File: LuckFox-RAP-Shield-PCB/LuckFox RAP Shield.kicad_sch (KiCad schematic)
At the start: 4 parts, among them J1 LuckFox_Pico_Mini_Connector, J2 External_5V_Input_from_Buck_M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, U2 W5500_Ethernet_Module_DNP_on_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

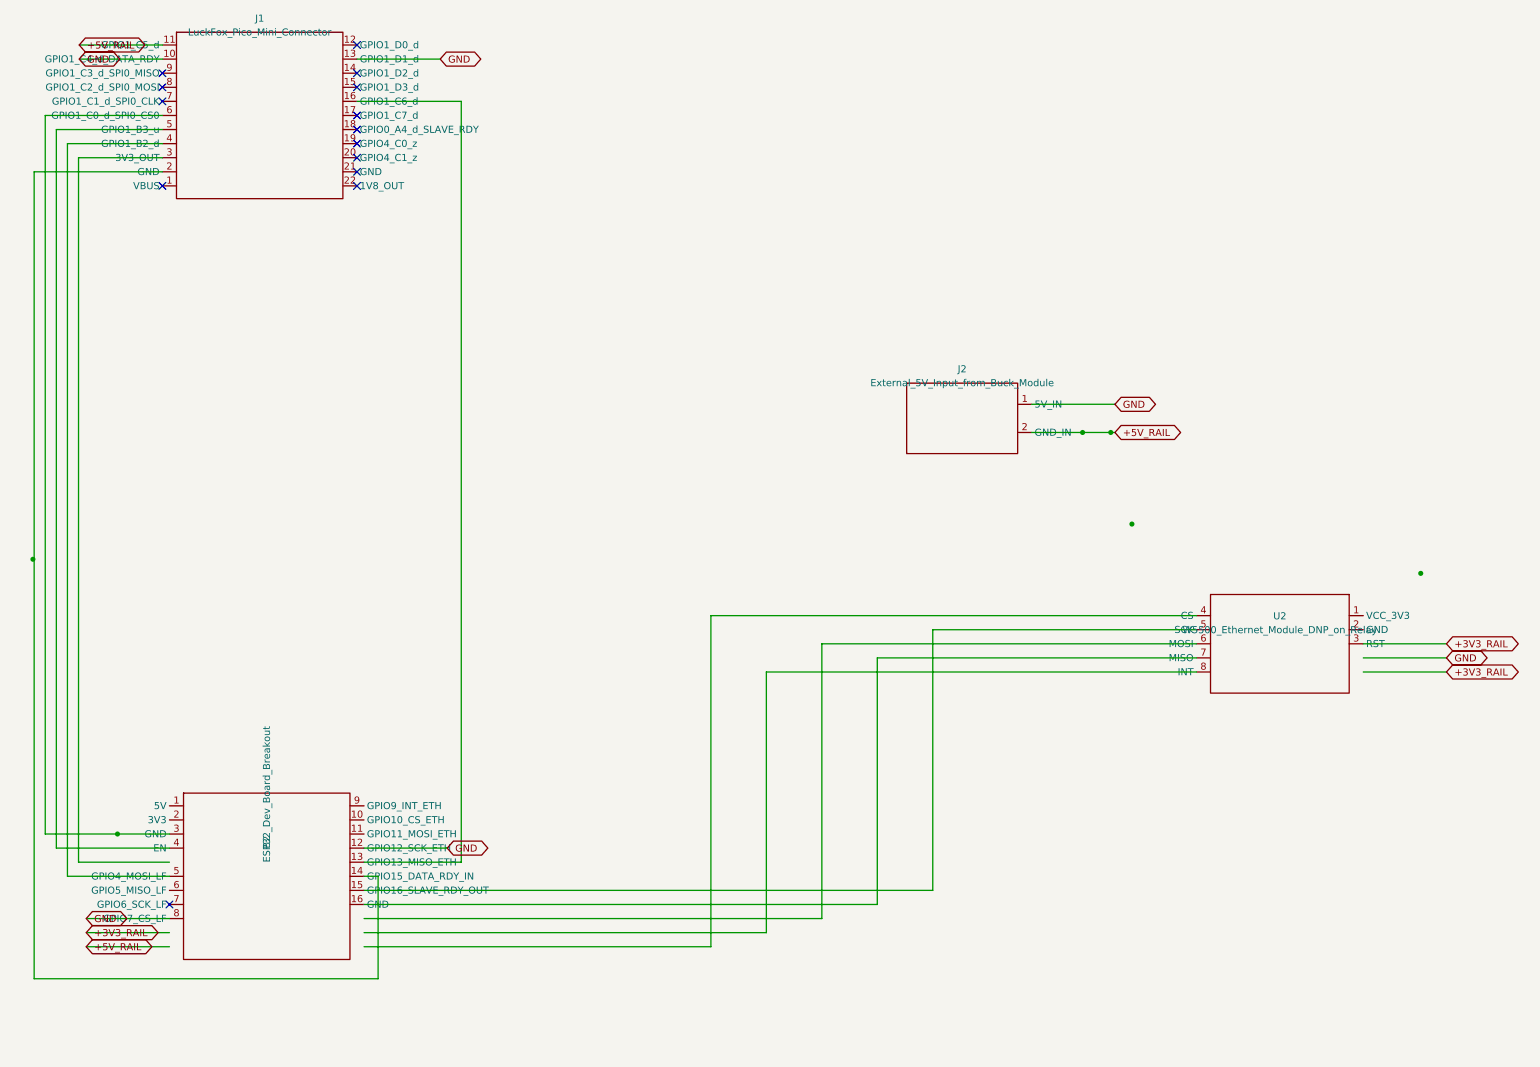
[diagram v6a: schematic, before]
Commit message: Manual wiring fixes in KiCad; switch J1 to castellated cutout mount
Schematic: incorporates your manual fixes in the KiCad GUI (component
repositioning, mirror/rotation adjustments) that brought ERC down from
141 to 14 messages, mostly remaining "not driven" warnings (expected
for global-label-based power rails without an explicit PWR_FLAG, not
real breaks). One genuine wire_dangling remains on the DATA_RDY-ish
net -- left for direct fixup in the GUI since positions were hand-
adjusted and no longer match a clean re-derivable formula.

Footprint: LuckFox_Pico_Mini.kicad_mod rebuilt from a through-hole
socket into a board-cutout + edge-castellation mount. LuckFox nests
underneath the shield (component side up) through a slot sized to its
21.00x28.14mm outline (+0.15mm clearance per side); its 22 castellated
edge pads lap-solder directly to matching pads straddling the cutout
edge on the shield's bottom copper -- no header/socket part at all.
Pad pitch/row-spacing (2.54mm / 17.78mm) match LuckFox's own pad grid,
per its official mechanical drawing. J1's schematic symbol/netlist is
unchanged; only the footprint (mechanical mounting) differs.
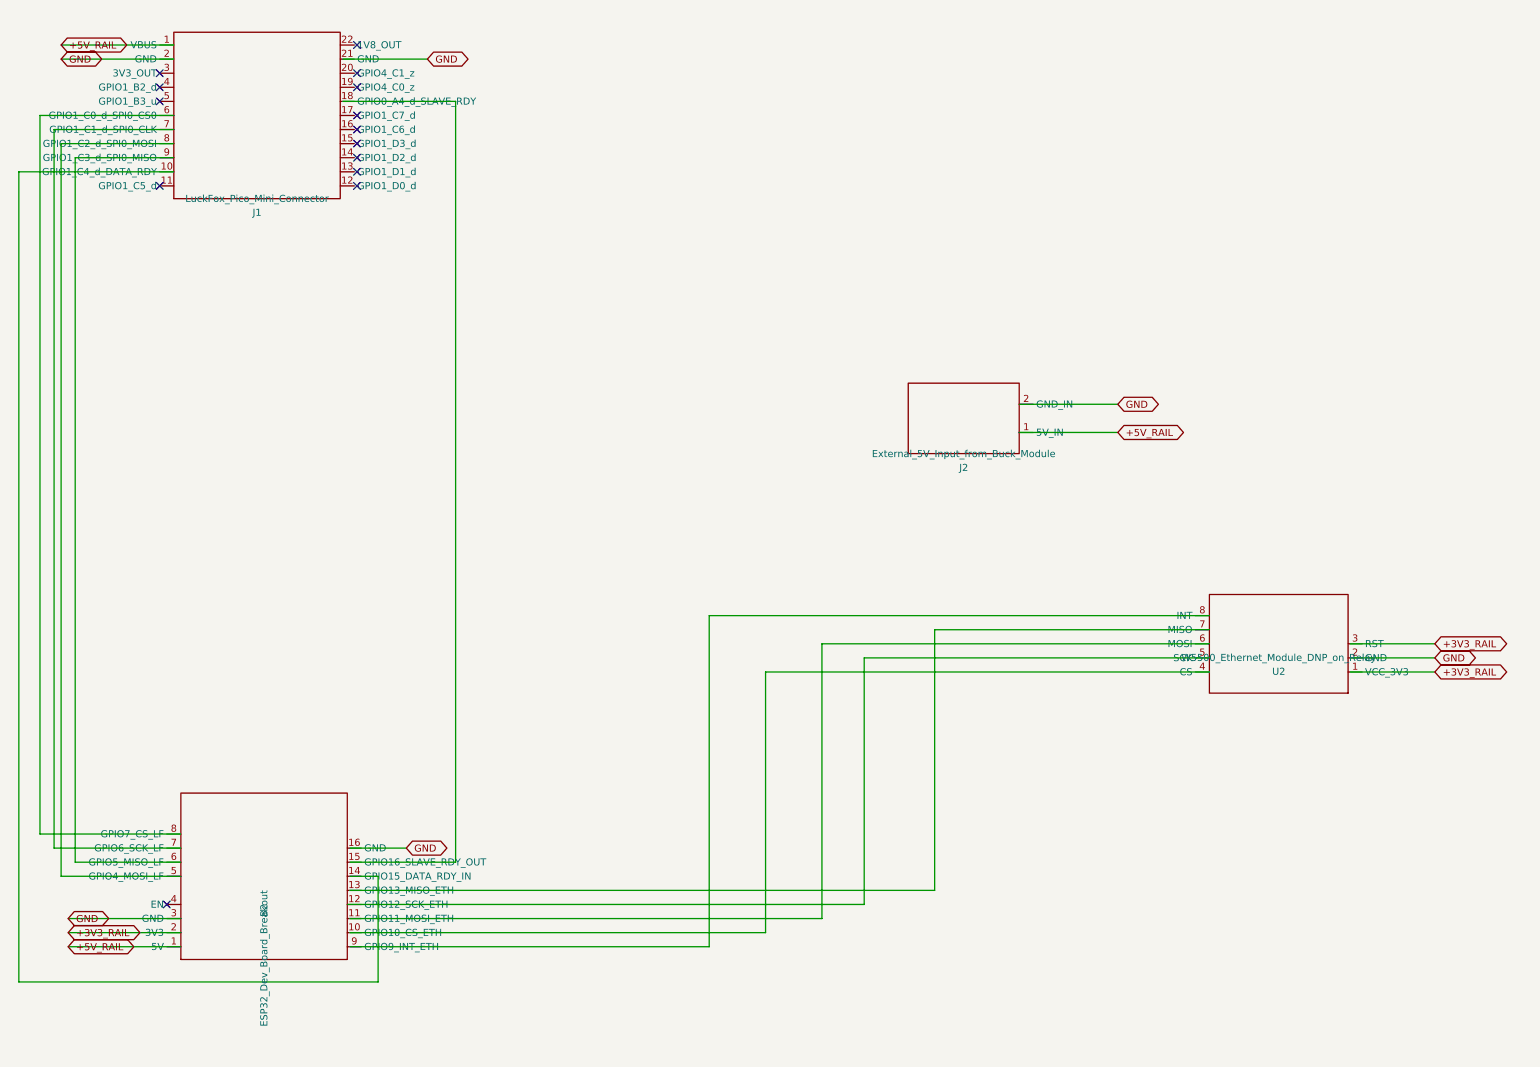
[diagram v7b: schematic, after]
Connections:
- net +3V3_RAIL: now also B2.2 (3V3)
- net +5V_RAIL: now also B2.1 (5V), J1.1 (VBUS), J2.1 (5V_IN)
- net GND: now also B2.3 (GND), J1.2 (GND), J2.2 (GND_IN)
- net at B2.12 (GPIO12_SCK_ETH): now also U2.5 (SCK)
- net at B2.5 (GPIO4_MOSI_LF): now also J1.8 (GPIO1_C2_d_SPI0_MOSI)
- net at B2.6 (GPIO5_MISO_LF): now also J1.9 (GPIO1_C3_d_SPI0_MISO)
- net at B2.7 (GPIO6_SCK_LF): now also J1.7 (GPIO1_C1_d_SPI0_CLK)
- net at B2.8 (GPIO7_CS_LF): now also J1.6 (GPIO1_C0_d_SPI0_CS0)
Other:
- moved on the sheet: U2

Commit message: Redraw all wiring to match current component positions/rotations
All 47 wires and 14 no_connect flags were stale, drawn against B2/J1/
J2/U2 positions from before several rounds of manual mirror/rotate/
move edits in the KiCad GUI. Confirmed with a brute-force check (every
mirror hypothesis, every component, against real wire endpoints):
zero matches anywhere, including U2's simple rotate-180-no-mirror
case -- not a transform-formula bug, the wires just didn't follow the
moves.

Recomputed every pin's true current absolute position (mirror- and
rotation-aware) and every pin's true exit direction, then redrew all
14 nets (SPI0, SPI-ETH, +5V_RAIL, +3V3_RAIL, GND) and all 13
intentionally-unused no_connect flags from scratch at those positions.
Verified with the same mirror-aware tracer: 14/14 nets correct, zero
stray or unconnected pins.
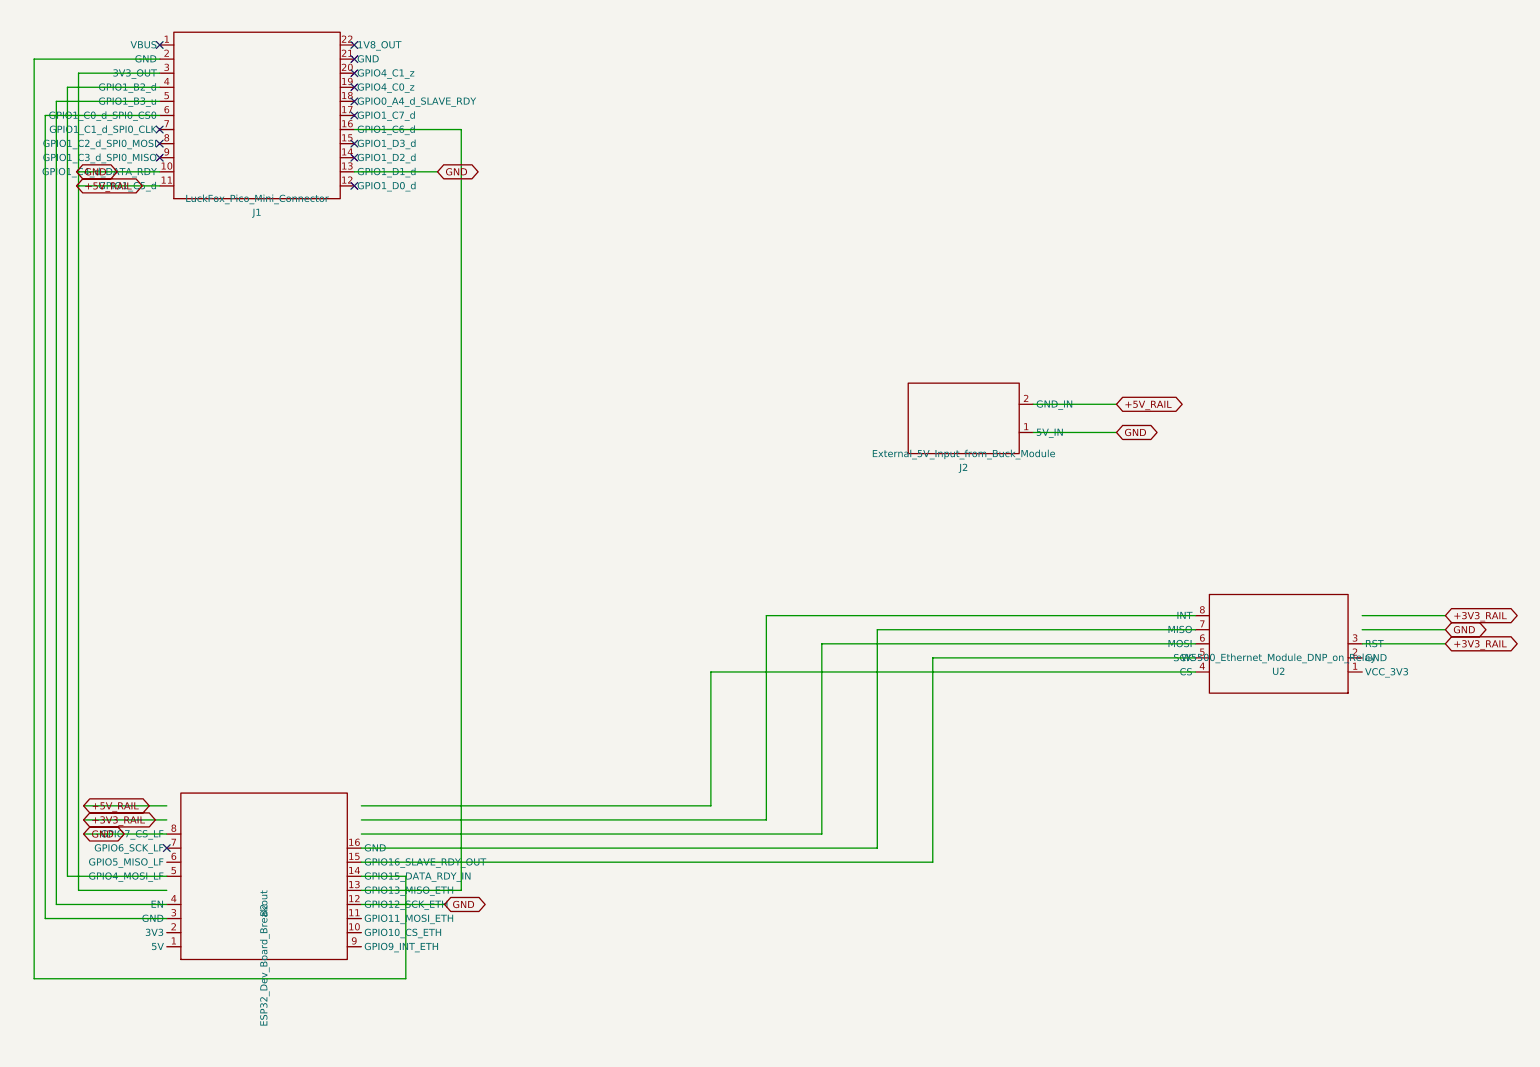
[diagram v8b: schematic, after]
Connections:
- net +3V3_RAIL: no longer B2.2 (3V3)
- net +5V_RAIL: no longer B2.1 (5V), J1.1 (VBUS), J2.1 (5V_IN)
- net GND: no longer B2.3 (GND), J1.2 (GND), J2.2 (GND_IN)
- net at B2.12 (GPIO12_SCK_ETH): no longer U2.5 (SCK)
- net at B2.5 (GPIO4_MOSI_LF): no longer J1.8 (GPIO1_C2_d_SPI0_MOSI)
- net at B2.6 (GPIO5_MISO_LF): no longer J1.9 (GPIO1_C3_d_SPI0_MISO)
- net at B2.7 (GPIO6_SCK_LF): no longer J1.7 (GPIO1_C1_d_SPI0_CLK)
- net at B2.8 (GPIO7_CS_LF): no longer J1.6 (GPIO1_C0_d_SPI0_CS0)
